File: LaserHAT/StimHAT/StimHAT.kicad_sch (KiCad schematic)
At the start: 123 parts, among them J1 GPIO, J10 OLED 0.91 (GND VCC SCL SDA), J101 ELECTRODE E1/E2, J102 B4B-PH-K-S(LF)(SN), J5 GT-USB-7010ASV, J6 BNC TRIGGER IN, J7 BNC STIM OUT, Q101 MMBT3904, Q102 MMBT3906, Q3 AP30P30Q, Q4 DMMT5401, Q5 AP30P30Q, SW10 MSK12C02, SW6 TS-1088-AR02016, SW7 SKRHADE010, SW9 TS-1088-AR02016, U1 M24C32-WDW6TP, U101 ISO7741FDBQR, U104 TLV76050DBZR, U105 DAC60501ZDGSR, U106 OPA2192IDGKR, U107 CD74HC4053PWR, U108 DG418DY-T1-E3, U109 ISO1640BDR, U110 TLV1702AIDGKR, U4 MCP1700T-3302E/MB, U5 AP2171W, U6 CH340N, U7 MSPM0G3507SRHBR, U8 74LVC2G17GW

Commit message: StimHAT: U7 = MSPM0G1507SRHBR (G3507 minus CAN-FD, same RHB pinout; LCSC code TODO)
Co-Authored-By: Claude Fable 5.1 <noreply@anthropic.com>
Claude-Session: https://claude.ai/code/session_015kiXLxnPpBaXdXJu2EMvn7
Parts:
- U7: value MSPM0G3507SRHBR -> MSPM0G1507SRHBR; LCSC Part # C20618748 -> (none); now left out of the parts list
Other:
- note added: "2. MSPM0G1507 (Rev 2 pin map; the G3507 minus CAN-FD, same RHB pinout), USB-UART (CH340N), RESET, BSL, JOYSTICK / FIRE, LEDs, 0.91 in OLED SOCKET"
- note removed: "2. MSPM0G3507 (Rev 2 pin map), USB-UART (CH340N), RESET, BSL, JOYSTICK / FIRE, LEDs, 0.91 in OLED SOCKET"
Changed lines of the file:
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@@
   )
   (rectangle (start 259.08 20.32) (end 508 157.48) (stroke (width 0.2) (type dash)) (fill (type none)))
-  (text "2. MSPM0G3507 (Rev 2 pin map), USB-UART (CH340N), RESET, BSL, JOYSTICK / FIRE, LEDs, 0.91 in OLED SOCKET" (exclude_from_sim no) (at 260.35 24.13 0) (effects (font (size 2.0 2.0) (bold yes)) (justify left bottom)))
-  (symbol (lib_id "stimhat:MSPM0G3507") (at 386.08 81.28 0) (unit 1) (exclude_from_sim no) (in_bom yes) (on_board yes) (dnp no)
+  (text "2. MSPM0G1507 (Rev 2 pin map; the G3507 minus CAN-FD, same RHB pinout), USB-UART (CH340N), RESET, BSL, JOYSTICK / FIRE, LEDs, 0.91 in OLED SOCKET" (exclude_from_sim no) (at 260.35 24.13 0) (effects (font (size 2.0 2.0) (bold yes)) (justify left bottom)))
+  (symbol (lib_id "stimhat:MSPM0G3507") (at 386.08 81.28 0) (unit 1) (exclude_from_sim no) (in_bom no) (on_board yes) (dnp no)
     (property "Reference" "U7" (at 386.08 57.15  0) (effects (font (size 1.27 1.27)) ))
-    (property "Value" "MSPM0G3507SRHBR" (at 386.08 105.41  0) (effects (font (size 1.27 1.27)) ))
+    (property "Value" "MSPM0G1507SRHBR" (at 386.08 105.41  0) (effects (font (size 1.27 1.27)) ))
     (property "Footprint" "stimhat:VQFN32_RHB_TEX" (at 386.08 81.28 0) (effects (font (size 1.27 1.27)) (hide yes)))
     (property "Datasheet" "" (at 386.08 81.28 0) (effects (font (size 1.27 1.27)) (hide yes)))
-    (property "LCSC Part #" "C20618748" (at 386.08 81.28 0) (effects (font (size 1.27 1.27)) (hide yes)))
     (pin "1")
     (pin "2")

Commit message: StimHAT: U7 LCSC C22406180 (MSPM0G1507SRHBR); bonnet outline, holes, socket, OLED, joystick and buttons on user layer Bonnet (from Adafruit's EagleCAD)
Co-Authored-By: Claude Fable 5.1 <noreply@anthropic.com>
Claude-Session: https://claude.ai/code/session_015kiXLxnPpBaXdXJu2EMvn7
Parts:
- U7: LCSC Part # (none) -> C22406180; now in the parts list
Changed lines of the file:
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@@
   (rectangle (start 259.08 20.32) (end 508 157.48) (stroke (width 0.2) (type dash)) (fill (type none)))
   (text "2. MSPM0G1507 (Rev 2 pin map; the G3507 minus CAN-FD, same RHB pinout), USB-UART (CH340N), RESET, BSL, JOYSTICK / FIRE, LEDs, 0.91 in OLED SOCKET" (exclude_from_sim no) (at 260.35 24.13 0) (effects (font (size 2.0 2.0) (bold yes)) (justify left bottom)))
-  (symbol (lib_id "stimhat:MSPM0G3507") (at 386.08 81.28 0) (unit 1) (exclude_from_sim no) (in_bom no) (on_board yes) (dnp no)
+  (symbol (lib_id "stimhat:MSPM0G3507") (at 386.08 81.28 0) (unit 1) (exclude_from_sim no) (in_bom yes) (on_board yes) (dnp no)
     (property "Reference" "U7" (at 386.08 57.15  0) (effects (font (size 1.27 1.27)) ))
     (property "Value" "MSPM0G1507SRHBR" (at 386.08 105.41  0) (effects (font (size 1.27 1.27)) ))
     (property "Footprint" "stimhat:VQFN32_RHB_TEX" (at 386.08 81.28 0) (effects (font (size 1.27 1.27)) (hide yes)))
     (property "Datasheet" "" (at 386.08 81.28 0) (effects (font (size 1.27 1.27)) (hide yes)))
+    (property "LCSC Part #" "C22406180" (at 386.08 81.28 0) (effects (font (size 1.27 1.27)) (hide yes)))
     (pin "1")
     (pin "2")

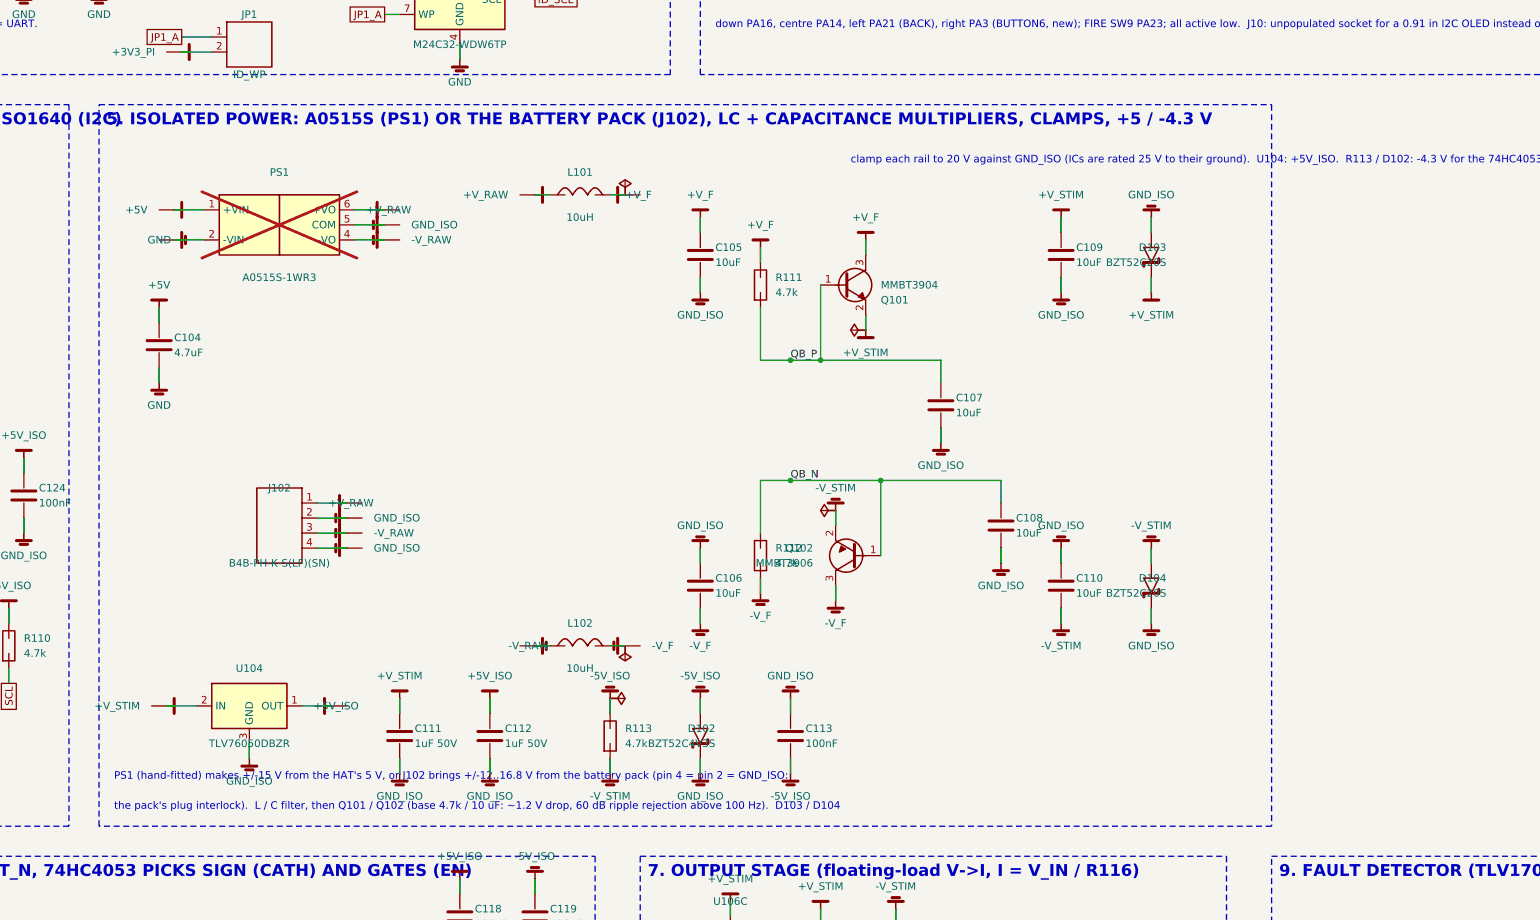
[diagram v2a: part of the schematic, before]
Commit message: StimHAT: isolated supply moves to a plug-in DC-DC pod - PS1, C104, LC filter and capacitance multipliers removed, J102 = +/-V_STIM input (pack cable or pod pins), J103 2-pin 5 V for the pod on the HAT side of the band; README pod spec
Co-Authored-By: Claude Fable 5.1 <noreply@anthropic.com>
Claude-Session: https://claude.ai/code/session_015kiXLxnPpBaXdXJu2EMvn7
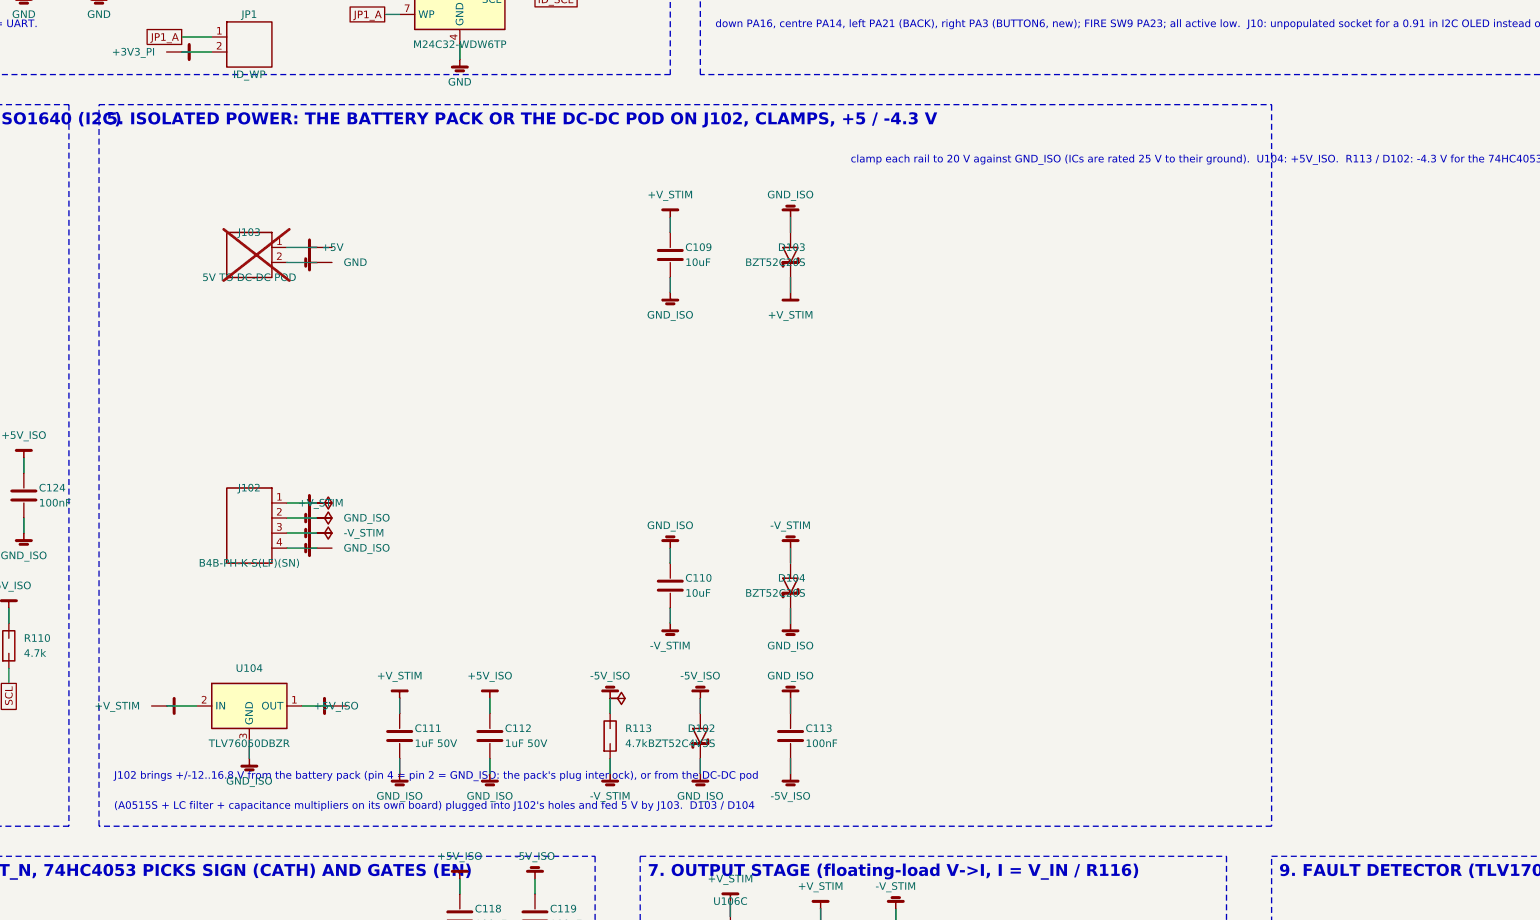
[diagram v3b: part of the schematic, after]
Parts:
- removed C104: 4.7uF, Capacitor_SMD:C_0603_1608Metric, symbol stimhat:C
- removed C105, C106, C107, C108: 10uF, Capacitor_SMD:C_0805_2012Metric, symbol stimhat:C
- removed L101, L102: 10uH, Inductor_SMD:L_0805_2012Metric, symbol stimhat:L
- removed PS1: A0515S-1WR3, stimhat:DCDC_SIP6_A0515S_BodyN, symbol stimhat:A0515S
- removed Q101: MMBT3904, Package_TO_SOT_SMD:SOT-23, symbol stimhat:Q_NPN_BEC
- removed Q102: MMBT3906, Package_TO_SOT_SMD:SOT-23, symbol stimhat:Q_PNP_BEC
- removed R111, R112: 4.7k, Resistor_SMD:R_0402_1005Metric, symbol stimhat:R
- added J103: 5V TO DC-DC POD, Connector_PinHeader_2.54mm:PinHeader_1x02_P2.54mm_Vertical, symbol stimhat:Conn_01x02
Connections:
- net +V_RAW is gone; now on net +V_STIM: J102.1 (Pin_1)
- net -V_RAW is gone; now on net -V_STIM: J102.3 (Pin_3)
- net +5V: now also J103.1 (Pin_1)
- net GND: now also J103.2 (Pin_2)
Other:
- note added: "(A0515S + LC filter + capacitance multipliers on its own board) plugged into J102's holes and fed 5 V by J103. D103 / D104"
- note added: "5. ISOLATED POWER: THE BATTERY PACK OR THE DC-DC POD ON J102, CLAMPS, +5 / -4.3 V"
- note added: "J102 brings +/-12..16.8 V from the battery pack (pin 4 = pin 2 = GND_ISO: the pack's plug interlock), or from the DC-DC pod"
- note removed: "5. ISOLATED POWER: A0515S (PS1) OR THE BATTERY PACK (J102), LC + CAPACITANCE MULTIPLIERS, CLAMPS, +5 / -4.3 V"
- note removed: "PS1 (hand-fitted) makes +/-15 V from the HAT's 5 V, or J102 brings +/-12..16.8 V from the battery pack (pin 4 = pin 2 = GND_ISO:"
- note removed: "the pack's plug interlock). L / C filter, then Q101 / Q102 (base 4.7k / 10 uF: ~1.2 V drop, 60 dB ripple rejection above 100 Hz). D103 / D104"
- moved on the sheet: C109, C110, D103, D104, J102
